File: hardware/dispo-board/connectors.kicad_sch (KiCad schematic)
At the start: 26 parts, among them J1 Conn_01x03, J10 Conn_01x02, J11 Conn_01x02, J12 Conn_01x03, J13 Conn_01x03, J14 Conn_ARM_JTAG_SWD_10, J2 Conn_01x03, J3 Conn_01x03, J4 Conn_01x04, J5 USB_B_Micro, J6 Conn_01x02, J7 Conn_01x02, J8 Conn_01x02, J9 Conn_01x02

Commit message: abgabe version
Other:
- note added: "TODO: proper analog input read section"
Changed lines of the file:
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@@
+		)
+	)
+	(text "TODO:\nproper analog input read section"
+		(exclude_from_sim no)
+		(at 317.754 29.464 0)
+		(effects
+			(font
+				(size 1.27 1.27)
+			)
 		)
 	)

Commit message: schematic should be ready, changed parts, ...
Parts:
- removed C20, C21, C22: 1u, Capacitor_SMD:C_0603_1608Metric, symbol Device:C
- removed J5: USB_B_Micro, Connector_USB:USB_Micro-B_Molex_47346-0001, symbol Connector:USB_B_Micro
- added C37, C39, C40: 1u, Capacitor_SMD:C_0402_1005Metric, symbol Device:C
- added J15: USB_B_Micro, Connector_USB:USB_Micro-B_Molex_47346-0001, symbol Connector:USB_B_Micro
- C23: footprint Capacitor_SMD:C_0603_1608Metric -> Capacitor_SMD:C_0402_1005Metric; MOUSER_NR 81-GRM185R61C105KE4J -> 963-LMK105BJ105MVHF
- R10, R11, R6, R7, R8, R9: MOUSER_NR 71-CRCW040210K0FKEDC -> 652-CR0402-JW-103GLF
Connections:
- net DIG_IN1: now also C23.1
- net DIG_IN2: now also C37.1
- net DIG_IN3: now also C39.1
- net DIG_IN4: now also C40.1; no longer C23.1
- net GND: now also C37.2, C39.2, C40.2, J15.5 (GND), J15.6 (Shield)
- net USBD+: now also J15.3 (D+)
- net USBD-: now also J15.2 (D-)
- net GUITAR_IN_P renamed GUITAR_IN
- net GUITAR_OUT_P renamed GUITAR_OUT
- new net 5V_USB: J15.1 (VBUS)
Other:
- moved on the sheet: J1, J12, J14, J4, J6

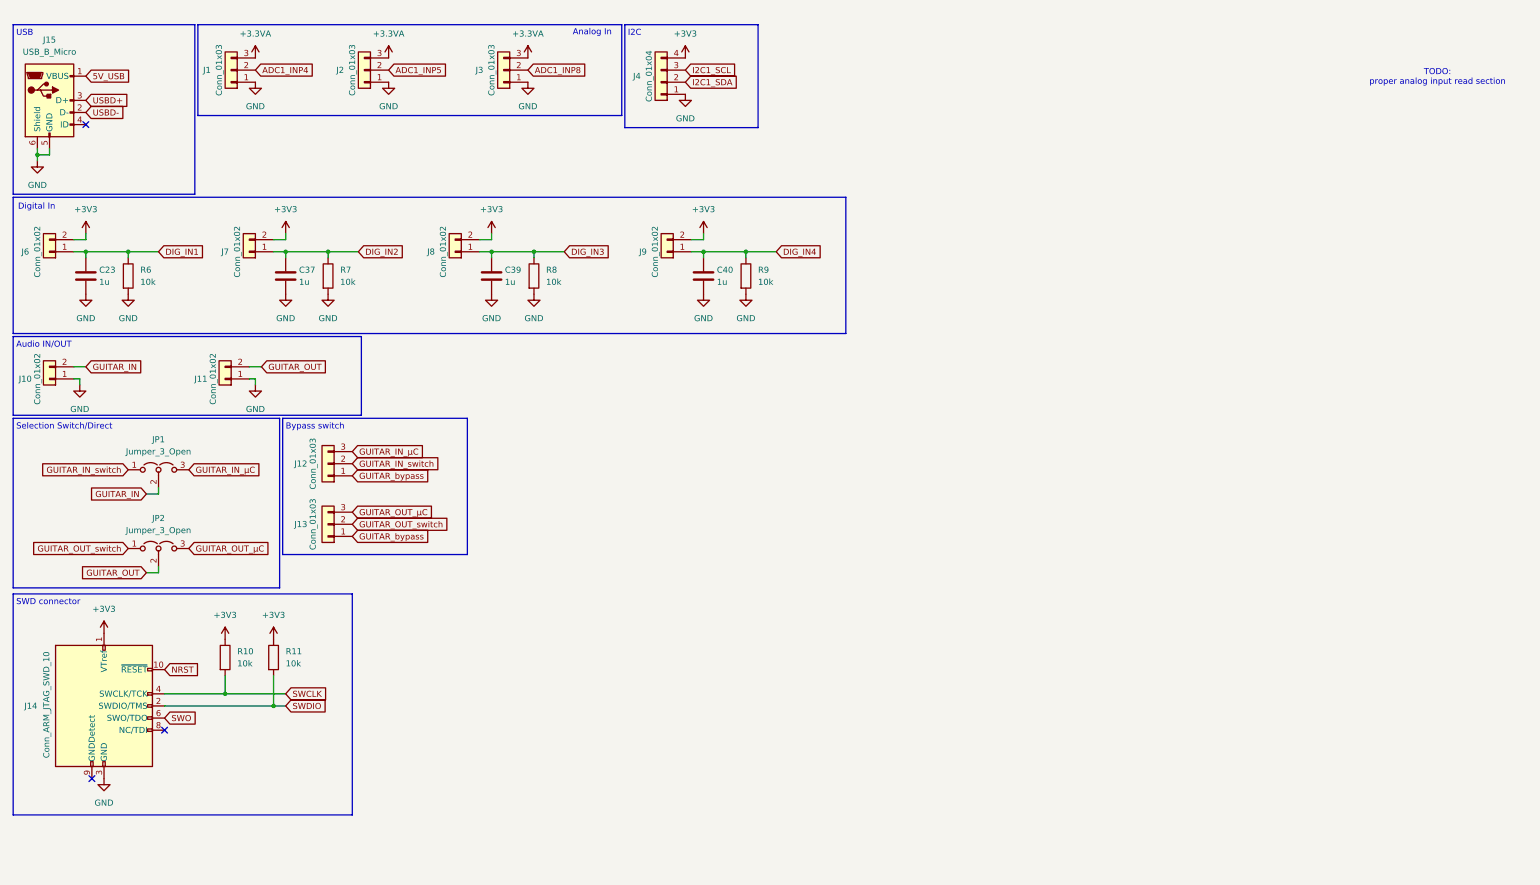
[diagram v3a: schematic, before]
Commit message: deleted nucleo board files, schematic ready?, changed to usb c
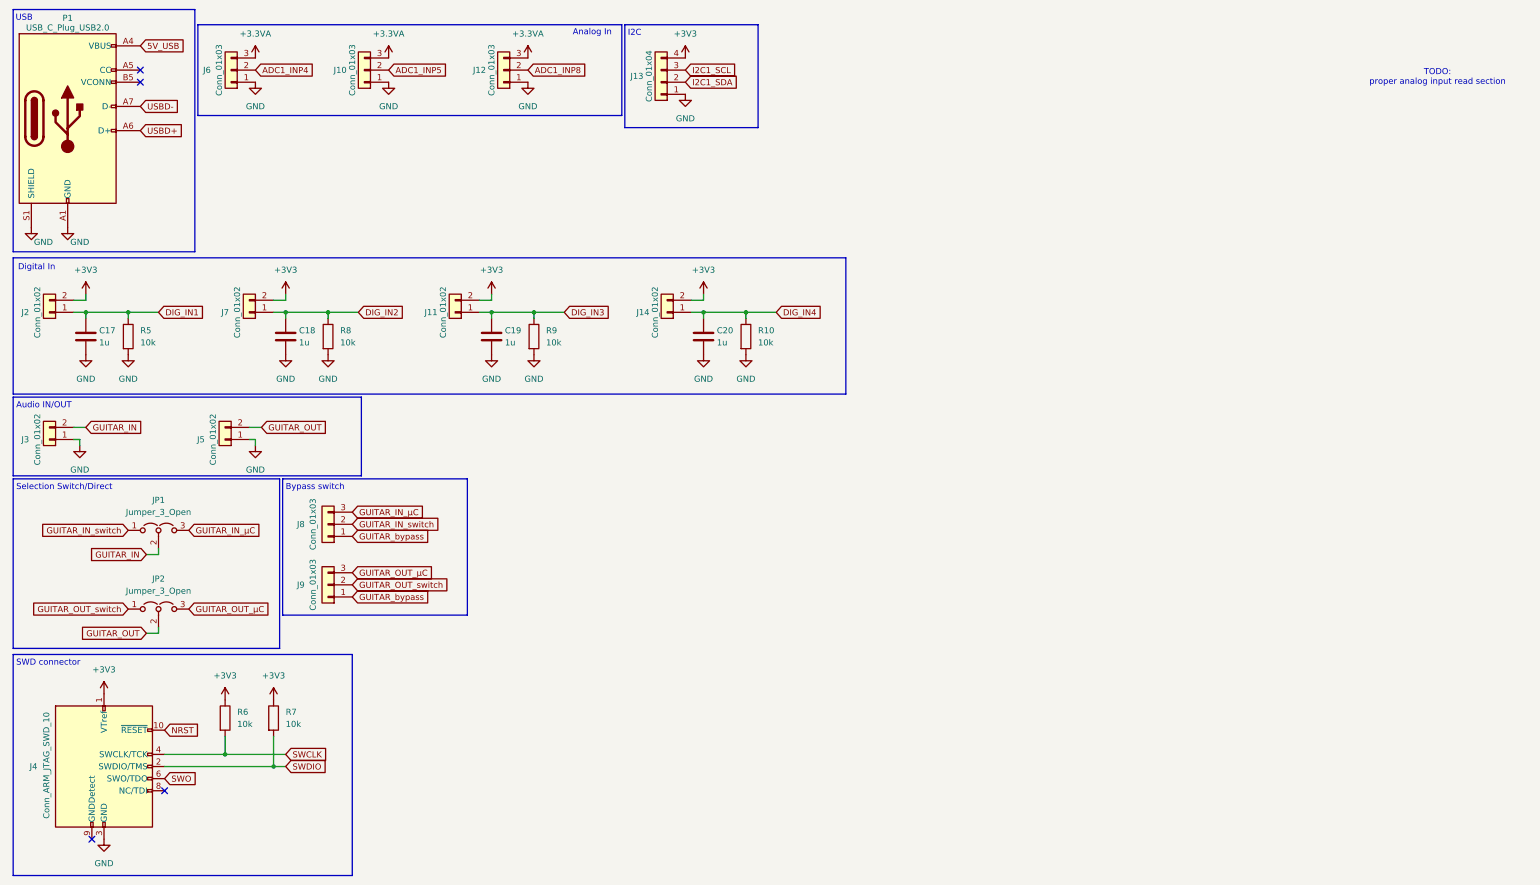
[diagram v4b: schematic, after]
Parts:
- removed J15: USB_B_Micro, Connector_USB:USB_Micro-B_Molex_47346-0001, symbol Connector:USB_B_Micro
- added P1: USB_C_Plug_USB2.0, Connector_USB:USB_C_Receptacle_JAE_DX07S016JA1R1500, symbol Connector:USB_C_Plug_USB2.0
- renumbered C23 to C17, C37 to C18, C39 to C19, C40 to C20, J2 to J10, J8 to J11, J3 to J12, J4 to J13, J9 to J14, J6 to J2, J10 to J3, J14 to J4, J11 to J5, J1 to J6, J12 to J8, J13 to J9, R9 to R10, R6 to R5, R10 to R6, R11 to R7, R7 to R8, R8 to R9
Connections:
- net 5V_USB: now also P1.A4 (VBUS), P1.A9 (VBUS), P1.B4 (VBUS), P1.B9 (VBUS)
- net GND: now also P1.A1 (GND), P1.A12 (GND), P1.B1 (GND), P1.B12 (GND), P1.S1 (SHIELD)
- net USBD+: now also P1.A6 (D+)
- net USBD-: now also P1.A7 (D-)
- no-connect marks 3 -> 4
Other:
- moved on the sheet: C17, C18, C19, C20, J11, J14, J2, J3, J4, J5, J7, J8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

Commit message: annotate schmetic
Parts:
- renumbered J2 to J1, J11 to J10, J12 to J11, J13 to J12, J14 to J13, J3 to J2, J4 to J3, J5 to J4, J6 to J5, J7 to J6, J8 to J7, J9 to J8, J10 to J9

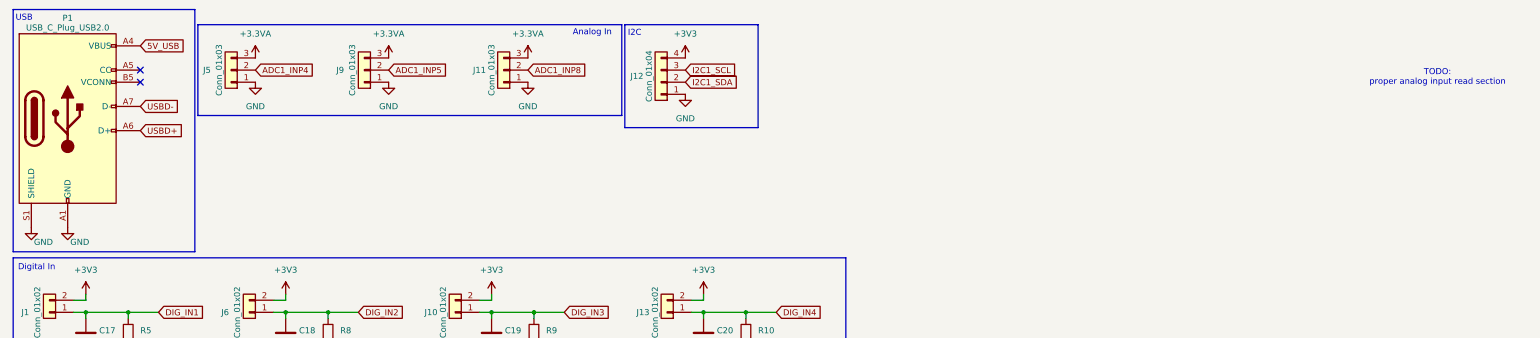
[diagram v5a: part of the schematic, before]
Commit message: changed again to micro usb, resolved spacing issues
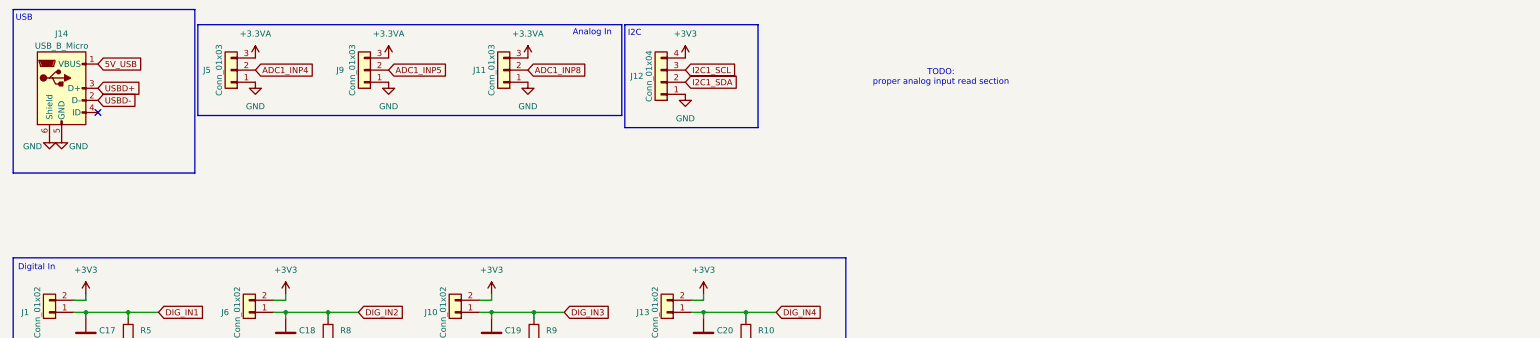
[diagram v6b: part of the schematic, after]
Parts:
- removed P1: USB_C_Plug_USB2.0, Connector_USB:USB_C_Receptacle_JAE_DX07S016JA1R1500, symbol Connector:USB_C_Plug_USB2.0
- added J14: USB_B_Micro, Connector_USB:USB_Micro-B_Molex_47346-0001, symbol Connector:USB_B_Micro
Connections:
- net 5V_USB: now also J14.1 (VBUS)
- net GND: now also J14.5 (GND), J14.6 (Shield)
- net USBD+: now also J14.3 (D+)
- net USBD-: now also J14.2 (D-)
- no-connect marks 4 -> 3
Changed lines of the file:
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@@
 	(rectangle
 		(start 19.05 15.24)
-		(end 57.15 66.04)
+		(end 57.15 49.53)
 		(stroke
 			(width 0)
@@
 	(text "TODO:\nproper analog input read section"
 		(exclude_from_sim no)
-		(at 317.754 29.464 0)
+		(at 213.614 29.464 0)
 		(effects
 			(font
@@
 	)
 	(no_connect
-		(at 45.72 30.48)
-	)
-	(no_connect
-		(at 45.72 27.94)
+		(at 36.83 36.83)
 	)
 	(no_connect
@@
 	(global_label "USBD-"
 		(shape input)
-		(at 45.72 35.56 0)
+		(at 36.83 34.29 0)
 		(fields_autoplaced yes)
 		(effects
@@
 		)
 		(property "Intersheetrefs" "${INTERSHEET_REFS}"
-			(at 55.3576 35.56 0)
+			(at 46.4676 34.29 0)
 			(effects
 				(font
@@
 	(global_label "5V_USB"
 		(shape input)
-		(at 45.72 22.86 0)
+		(at 36.83 26.67 0)
 		(fields_autoplaced yes)
 		(effects
@@
 		)
 		(property "Intersheetrefs" "${INTERSHEET_REFS}"
-			(at 55.7809 22.86 0)
+			(at 46.8909 26.67 0)
 			(effects
 				(font
@@
 	(global_label "USBD+"
 		(shape input)
-		(at 45.72 40.64 0)
+		(at 36.83 31.75 0)
 		(fields_autoplaced yes)
 		(effects
@@
 		)
 		(property "Intersheetrefs" "${INTERSHEET_REFS}"
-			(at 55.3576 40.64 0)
+			(at 46.4676 31.75 0)
 			(effects
 				(font
@@
 	(symbol
 		(lib_id "power:GND")
-		(at 30.48 60.96 0)
+		(at 29.21 41.91 0)
 		(unit 1)
 		(exclude_from_sim no)
@@
 		(dnp no)
 		(property "Reference" "#PWR024"
-			(at 30.48 67.31 0)
+			(at 29.21 48.26 0)
 			(effects
 				(font
@@
 		)
 		(property "Value" "GND"
-			(at 33.02 64.008 0)
+			(at 32.766 43.942 0)
 			(effects
 				(font
@@
 		)
 		(property "Footprint" ""
-			(at 30.48 60.96 0)
+			(at 29.21 41.91 0)
 			(effects
 				(font
@@
 		)
 		(property "Datasheet" ""
-			(at 30.48 60.96 0)
+			(at 29.21 41.91 0)
 			(effects
 				(font
@@
 		)
 		(property "Description" "Power symbol creates a global label with name \"GND\" , ground"
-			(at 30.48 60.96 0)
+			(at 29.21 41.91 0)
 			(effects
 				(font
@@
 	)
 	(symbol
-		(lib_id "Connector:USB_C_Plug_USB2.0")
-		(at 30.48 38.1 0)
-		(unit 1)
-		(exclude_from_sim no)
-		(in_bom yes)
-		(on_board yes)
-		(dnp no)
-		(property "Reference" "P1"
-			(at 30.48 17.018 0)
-			(effects
-				(font
-					(size 1.27 1.27)
-				)
-			)
-		)
-		(property "Value" "USB_C_Plug_USB2.0"
-			(at 30.48 19.05 0)
-			(effects
-				(font
-					(size 1.27 1.27)
-				)
-			)
-		)
-		(property "Footprint" "Connector_USB:USB_C_Receptacle_JAE_DX07S016JA1R1500"
-			(at 34.29 38.1 0)
-			(effects
-				(font
-					(size 1.27 1.27)
-				)
-				(hide yes)
-			)
-		)
-		(property "Datasheet" "https://www.usb.org/sites/default/files/documents/usb_type-c.zip"
-			(at 34.29 38.1 0)
-			(effects
-				(font
-					(size 1.27 1.27)
-				)
-				(hide yes)
-			)
-		)
-		(property "Description" "USB 2.0-only Type-C Plug connector"
-			(at 30.48 38.1 0)
-			(effects
-				(font
-					(size 1.27 1.27)
-				)
-				(hide yes)
-			)
-		)
-		(property "MOUSER_NR" "656-DX07S016JA1R1500"
-			(at 30.48 38.1 0)
-			(effects
-				(font
-					(size 1.27 1.27)
-				)
-				(hide yes)
-			)
-		)
-		(pin "B12"
-		)
-		(pin "A6"
-		)
-		(pin "B5"
-		)
-		(pin "A4"
-		)
-		(pin "B4"
-		)
-		(pin "A5"
-		)
-		(pin "A1"
-		)
-		(pin "A7"
-		)
-		(pin "S1"
-		)
-		(pin "B9"
-		)
-		(pin "A12"
-		)
-		(pin "A9"
-		)
-		(pin "B1"
-		)
-		(instances
-			(project ""
-				(path "/93ea4da8-8485-4fb5-a89d-c72021d94c09/b8888756-c15f-4275-bc58-daa9bb032a86"
-					(reference "P1")
-					(unit 1)
-				)
-			)
-		)
-	)
-	(symbol
 		(lib_id "Jumper:Jumper_3_Open")
 		(at 49.53 140.97 0)
@@
 	(symbol
 		(lib_id "power:GND")
-		(at 22.86 60.96 0)
+		(at 26.67 41.91 0)
 		(unit 1)
 		(exclude_from_sim no)
@@
 		(dnp no)
 		(property "Reference" "#PWR023"
-			(at 22.86 67.31 0)
+			(at 26.67 48.26 0)
 			(effects
 				(font
@@
 		)
 		(property "Value" "GND"
-			(at 25.4 64.008 0)
+			(at 23.114 43.942 0)
 			(effects
 				(font
@@
 		)
 		(property "Footprint" ""
-			(at 22.86 60.96 0)
+			(at 26.67 41.91 0)
 			(effects
 				(font
@@
 		)
 		(property "Datasheet" ""
-			(at 22.86 60.96 0)
+			(at 26.67 41.91 0)
 			(effects
 				(font
@@
 		)
 		(property "Description" "Power symbol creates a global label with name \"GND\" , ground"
-			(at 22.86 60.96 0)
+			(at 26.67 41.91 0)
 			(effects
 				(font
@@
 					(unit 1)
 				)
+			)
+		)
+	)
+	(symbol
+		(lib_id "Connector:USB_B_Micro")
+		(at 29.21 31.75 0)
+		(unit 1)
+		(exclude_from_sim no)
+		(in_bom yes)
+		(on_board yes)
+		(dnp no)
+		(fields_autoplaced yes)
+		(property "Reference" "J14"
+			(at 29.21 20.32 0)
+			(effects
+				(font
+					(size 1.27 1.27)
+				)
+			)
+		)
+		(property "Value" "USB_B_Micro"
+			(at 29.21 22.86 0)
+			(effects
+				(font
+					(size 1.27 1.27)
+				)
+			)
+		)
+		(property "Footprint" "Connector_USB:USB_Micro-B_Molex_47346-0001"
+			(at 33.02 33.02 0)
+			(effects
+				(font
+					(size 1.27 1.27)
+				)
+				(hide yes)
+			)
+		)
+		(property "Datasheet" "~"
+			(at 33.02 33.02 0)
+			(effects
+				(font
+					(size 1.27 1.27)
+				)
+				(hide yes)
+			)
+		)
+		(property "Description" "USB Micro Type B connector"
+			(at 29.21 31.75 0)
+			(effects
+				(font
+					(size 1.27 1.27)
+				)
+				(hide yes)
+			)
+		)
+		(property "MOUSER_NR" "538-47346-1001"
+			(at 29.21 31.75 0)
+			(effects
+				(font
+					(size 1.27 1.27)
+				)
+				(hide yes)
+			)
+		)
+		(pin "3"
+		)
+		(pin "2"
+		)
+		(pin "4"
+		)
+		(pin "1"
+		)
+		(pin "5"
+		)
+		(pin "6"
+		)
+		(instances
+			(project ""
+				(path "/93ea4da8-8485-4fb5-a89d-c72021d94c09/b8888756-c15f-4275-bc58-daa9bb032a86"
+					(reference "J14")
+					(unit 1)
+				)
